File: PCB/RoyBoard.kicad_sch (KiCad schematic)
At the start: 175 parts, among them SW1 SW_Push, SW10 SW_Push, SW11 SW_Push, SW12 SW_Push, SW13 SW_Push, SW14 SW_Push, SW15 SW_Push, SW16 SW_Push, SW17 SW_Push, SW18 SW_Push, SW19 SW_Push, SW2 SW_Push, SW20 SW_Push, SW21 SW_Push, SW22 SW_Push, SW23 SW_Push, SW24 SW_Push, SW25 SW_Push, SW26 SW_Push, SW27 SW_Push, SW28 SW_Push, SW29 SW_Push, SW3 SW_Push, SW30 SW_Push, SW31 SW_Push, SW32 SW_Push, SW33 SW_Push, SW34 SW_Push, SW35 SW_Push, SW36 SW_Push, SW37 SW_Push, SW38 SW_Push, SW39 SW_Push, SW4 SW_Push, SW40 SW_Push, SW41 SW_Push, SW42 SW_Push, SW43 SW_Push, SW44 SW_Push, SW45 SW_Push, SW46 SW_Push, SW47 SW_Push, SW48 SW_Push, SW49 SW_Push, SW5 SW_Push, SW50 SW_Push, SW51 SW_Push, SW52 SW_Push, SW53 SW_Push, SW54 SW_Push, SW55 SW_Push, SW56 SW_Push, SW57 SW_Push, SW58 SW_Push, SW59 SW_Push, SW6 SW_Push, SW60 SW_Push, SW61 SW_Push, SW62 SW_Push, SW63 SW_Push, SW64 SW_Push, SW65 SW_Push, SW66 SW_Push, SW67 SW_Push, SW68 SW_Push, SW69 SW_Push, SW7 SW_Push, SW70 SW_Push, SW71 SW_Push, SW72 SW_Push, SW73 SW_Push, SW74 SW_Push, SW75 SW_Push, SW76 SW_Push, SW77 SW_Push, SW78 SW_Push, SW79 SW_Push, SW8 SW_Push, SW80 SW_Push, SW81 SW_Push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

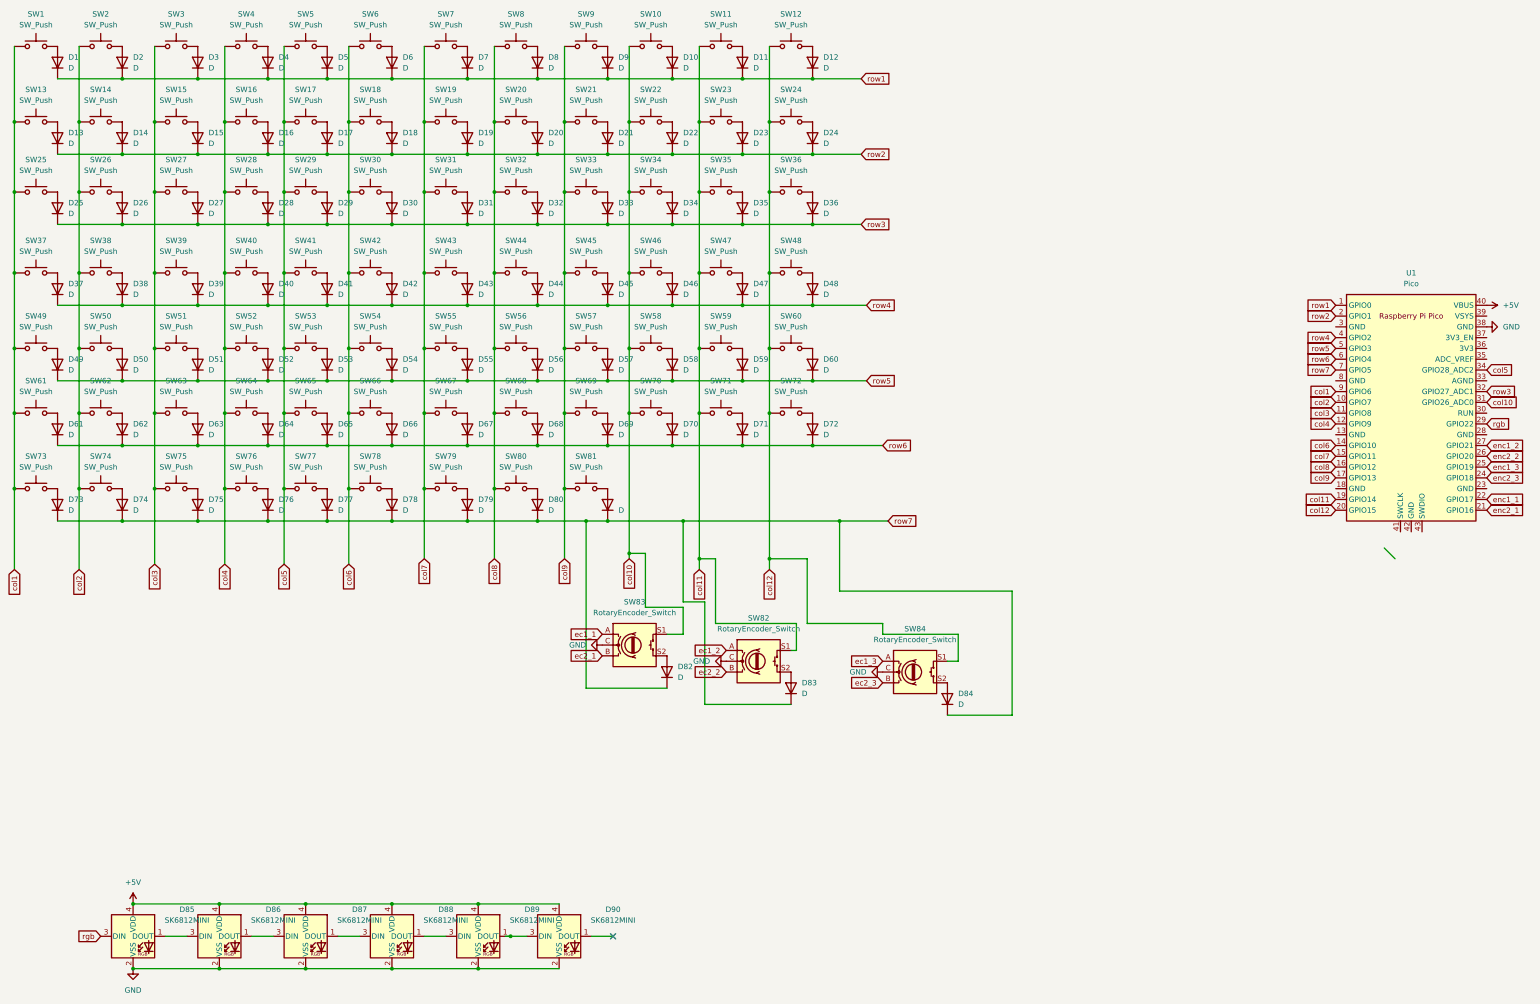
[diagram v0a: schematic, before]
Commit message: Added CAD models, firmware and 3d renders
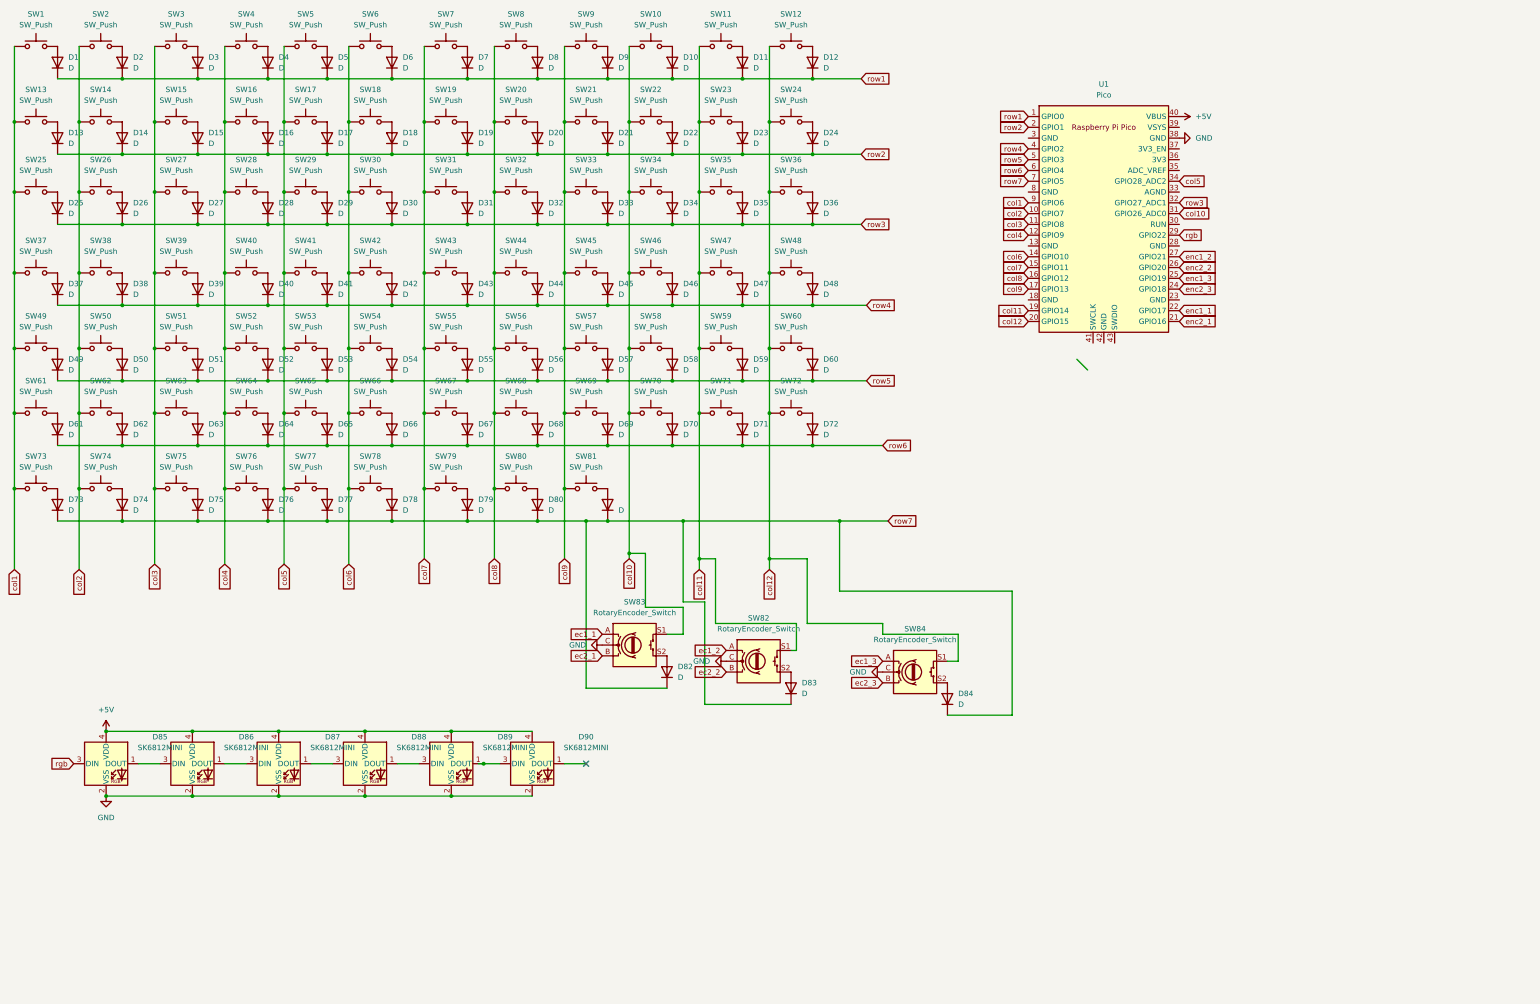
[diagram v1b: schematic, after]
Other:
- moved on the sheet: D85, D86, D87, D88, D89, D90, U1
